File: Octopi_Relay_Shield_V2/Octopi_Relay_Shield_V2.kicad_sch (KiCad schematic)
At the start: 11 parts, among them J1 Raspberry_Pi_2_3, J2 Screw_Terminal_01x03, K1 JQC-3FF-005-1Z, Q1 NPN, U1 LTV-817S

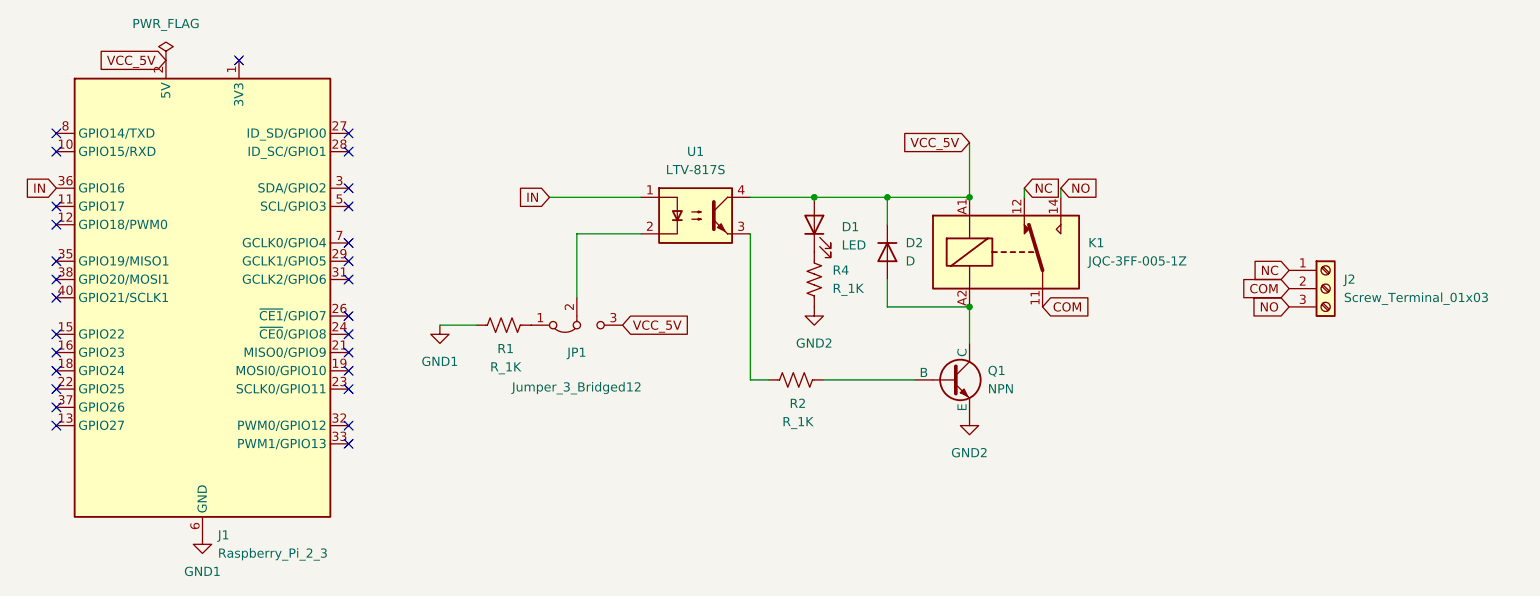
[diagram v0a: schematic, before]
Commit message: Completed Layout for first two designs, generated the fab files
updated the nets, GND1 and GND2 have been joined into just GND1. separated GNDs would only be possible if there was a separate non-pi voltage source for the 5V on the other side of the octocoupler
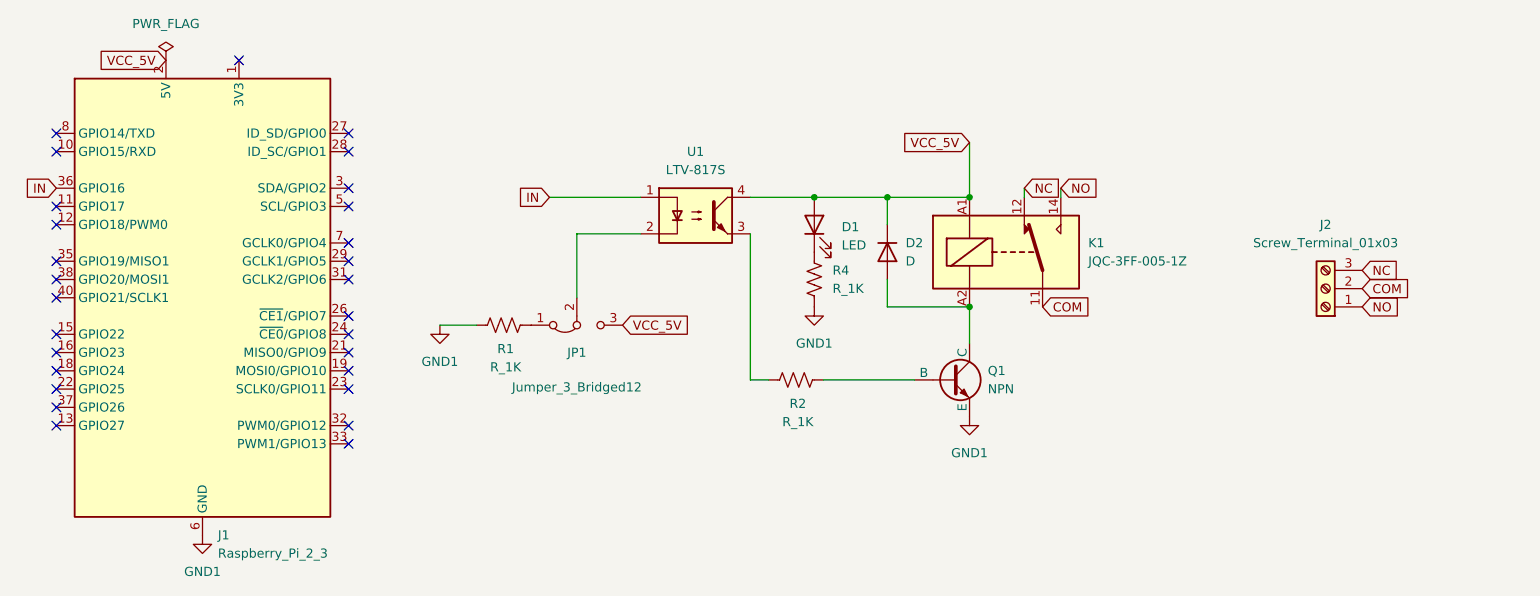
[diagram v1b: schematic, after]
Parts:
- D1: footprint LED_SMD:LED_0805_2012Metric_Pad1.15x1.40mm_HandSolder -> LED_SMD:LED_0603_1608Metric_Pad1.05x0.95mm_HandSolder
- D2: footprint Diode_SMD:D_0805_2012Metric_Pad1.15x1.40mm_HandSolder -> Diode_THT:D_5W_P12.70mm_Horizontal
- J1: footprint Connector_PinHeader_2.54mm:PinHeader_2x20_P2.54mm_Vertical -> Connector_PinSocket_2.54mm:PinSocket_2x20_P2.54mm_Vertical
- J2: footprint TerminalBlock_MetzConnect:TerminalBlock_MetzConnect_Type011_RT05503HBLC_1x03_P5.00mm_Horizontal -> TerminalBlock_Phoenix:TerminalBlock_Phoenix_PT-1,5-3-5.0-H_1x03_P5.00mm_Horizontal
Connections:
- net GND2 is gone; now on net GND1: Q1.3 (E), R4.2
- net NC: now also J2.3 (Pin_3); no longer J2.1 (Pin_1)
- net NO: now also J2.1 (Pin_1); no longer J2.3 (Pin_3)
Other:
- moved on the sheet: J2
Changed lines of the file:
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@@
 	(global_label "COM"
 		(shape input)
-		(at 201.93 73.66 180)
+		(at 212.09 73.66 0)
 		(fields_autoplaced yes)
 		(effects
@@
 				(size 1.27 1.27)
 			)
-			(justify right)
+			(justify left)
 		)
 		(property "Intersheetrefs" "${INTERSHEET_REFS}"
-			(at 194.8929 73.66 0)
-			(effects
-				(font
-					(size 1.27 1.27)
-				)
-				(justify right)
+			(at 219.1271 73.66 0)
+			(effects
+				(font
+					(size 1.27 1.27)
+				)
+				(justify left)
 				(hide yes)
 			)
@@
 	(global_label "NC"
 		(shape input)
-		(at 201.93 71.12 180)
+		(at 212.09 71.12 0)
 		(fields_autoplaced yes)
 		(effects
@@
 				(size 1.27 1.27)
 			)
-			(justify right)
+			(justify left)
 		)
 		(property "Intersheetrefs" "${INTERSHEET_REFS}"
-			(at 196.3443 71.12 0)
-			(effects
-				(font
-					(size 1.27 1.27)
-				)
-				(justify right)
+			(at 217.6757 71.12 0)
+			(effects
+				(font
+					(size 1.27 1.27)
+				)
+				(justify left)
 				(hide yes)
 			)
@@
 	(global_label "NO"
 		(shape input)
-		(at 201.93 76.2 180)
+		(at 212.09 76.2 0)
 		(fields_autoplaced yes)
 		(effects
@@
 				(size 1.27 1.27)
 			)
-			(justify right)
+			(justify left)
 		)
 		(property "Intersheetrefs" "${INTERSHEET_REFS}"
-			(at 196.2838 76.2 0)
-			(effects
-				(font
-					(size 1.27 1.27)
-				)
-				(justify right)
+			(at 217.7362 76.2 0)
+			(effects
+				(font
+					(size 1.27 1.27)
+				)
+				(justify left)
 				(hide yes)
 			)
@@
 			)
 		)
-		(property "Value" "GND2"
+		(property "Value" "GND1"
 			(at 135.89 81.28 0)
 			(effects
@@
 	(symbol
 		(lib_id "Connector:Screw_Terminal_01x03")
-		(at 207.01 73.66 0)
+		(at 207.01 73.66 180)
 		(unit 1)
 		(exclude_from_sim no)
@@
 		(fields_autoplaced yes)
 		(property "Reference" "J2"
-			(at 209.55 72.3899 0)
-			(effects
-				(font
-					(size 1.27 1.27)
-				)
-				(justify left)
+			(at 207.01 64.77 0)
+			(effects
+				(font
+					(size 1.27 1.27)
+				)
 			)
 		)
 		(property "Value" "Screw_Terminal_01x03"
-			(at 209.55 74.9299 0)
-			(effects
-				(font
-					(size 1.27 1.27)
-				)
-				(justify left)
-			)
-		)
-		(property "Footprint" "TerminalBlock_MetzConnect:TerminalBlock_MetzConnect_Type011_RT05503HBLC_1x03_P5.00mm_Horizontal"
+			(at 207.01 67.31 0)
+			(effects
+				(font
+					(size 1.27 1.27)
+				)
+			)
+		)
+		(property "Footprint" "TerminalBlock_Phoenix:TerminalBlock_Phoenix_PT-1,5-3-5.0-H_1x03_P5.00mm_Horizontal"
 			(at 207.01 73.66 0)
 			(effects
@@
 			)
 		)
-		(property "Footprint" "LED_SMD:LED_0805_2012Metric_Pad1.15x1.40mm_HandSolder"
+		(property "Footprint" "LED_SMD:LED_0603_1608Metric_Pad1.05x0.95mm_HandSolder"
 			(at 135.89 64.77 0)
 			(effects
@@
 			)
 		)
-		(property "Value" "GND2"
+		(property "Value" "GND1"
 			(at 157.48 96.52 0)
 			(effects
@@
 			)
 		)
-		(property "Footprint" "Diode_SMD:D_0805_2012Metric_Pad1.15x1.40mm_HandSolder"
+		(property "Footprint" "Diode_THT:D_5W_P12.70mm_Horizontal"
 			(at 146.05 68.58 0)
 			(effects
@@
 			)
 		)
-		(property "Footprint" "Connector_PinHeader_2.54mm:PinHeader_2x20_P2.54mm_Vertical"
+		(property "Footprint" "Connector_PinSocket_2.54mm:PinSocket_2x20_P2.54mm_Vertical"
 			(at 50.8 74.93 0)
 			(effects
